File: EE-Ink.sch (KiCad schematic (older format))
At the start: 26 parts, among them U1 ED060SC4

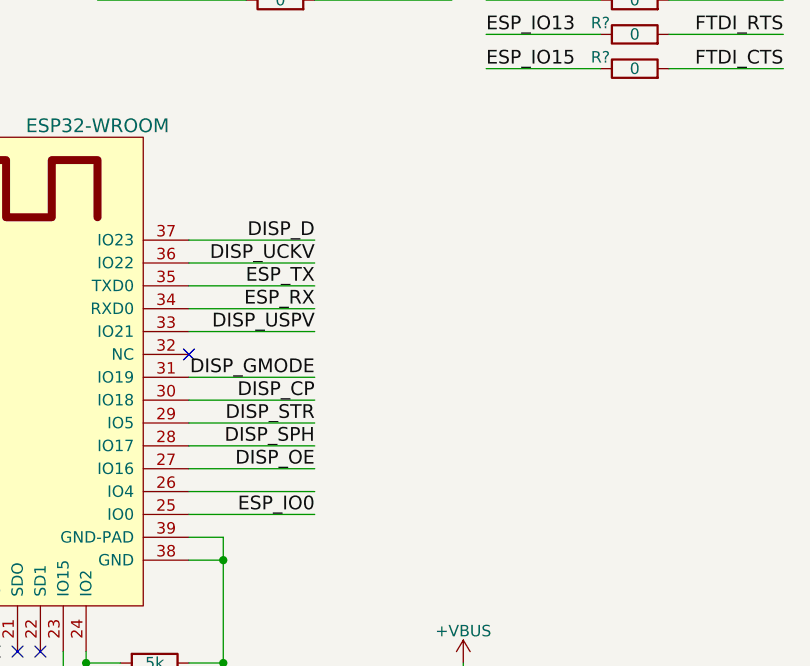
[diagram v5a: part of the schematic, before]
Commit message: Added status LED.
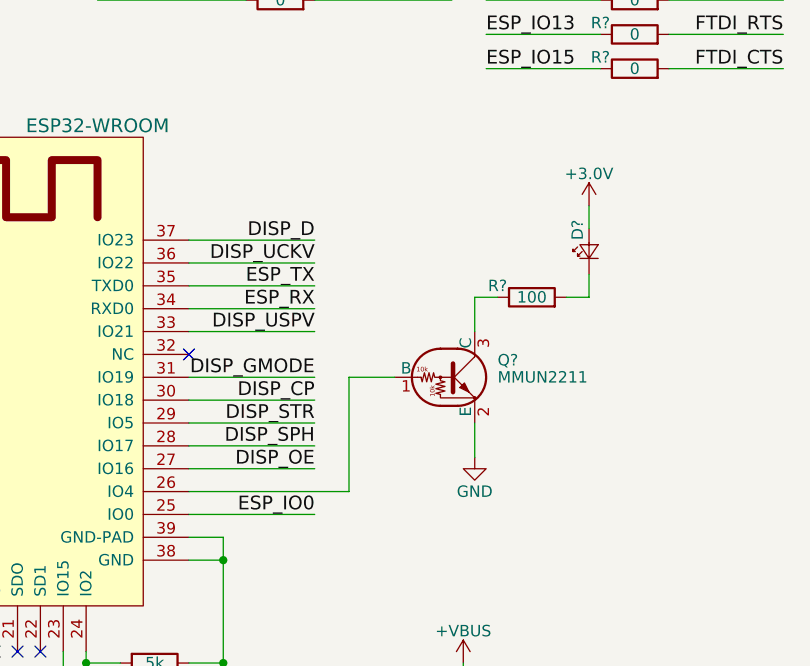
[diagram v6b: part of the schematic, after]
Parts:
- added D?: LED_Small, symbol LED_Small
- added Q?: MMUN2211, symbol DTC114E
- added R?: 100, symbol R
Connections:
- net +3.0V: now also D?.2 (A)
- net GND: now also Q?.2 (E)
- net at U?.26 (IO4): now also Q?.1 (B)
- new net: Q?.3 (C), R?.1
- new net: D?.1 (K), R?.2
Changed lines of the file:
@@
 	8300 3250 8850 3250
 Wire Wire Line
-	8300 3350 8850 3350
+	8300 3350 9000 3350
 $Comp
 L C_Small C?
@@
 	5350 4150 5350 4050
 Connection ~ 5350 4050
+$Comp
+L DTC114E Q?
+U 1 1 58E4DFD0
+P 9450 2850
+F 0 "Q?" H 9650 2925 50  0000 L CNN
+F 1 "MMUN2211" H 9650 2850 50  0000 L CNN
+F 2 "" H 9450 2850 50  0001 L CNN
+F 3 "" H 9450 2850 50  0001 L CNN
+	1    9450 2850
+	1    0    0    -1
+$EndComp
+$Comp
+L GND #PWR?
+U 1 1 58E4F157
+P 9550 3200
+F 0 "#PWR?" H 9550 2950 50  0001 C CNN
+F 1 "GND" H 9550 3050 50  0000 C CNN
+F 2 "" H 9550 3200 50  0001 C CNN
+F 3 "" H 9550 3200 50  0001 C CNN
+	1    9550 3200
+	1    0    0    -1
+$EndComp
+Wire Wire Line
+	9550 3050 9550 3200
+Wire Wire Line
+	9200 2850 9000 2850
+Wire Wire Line
+	9000 2850 9000 3350
+$Comp
+L R R?
+U 1 1 58E50804
+P 9800 2500
+F 0 "R?" V 9850 2650 50  0000 C CNN
+F 1 "100" V 9800 2500 50  0000 C CNN
+F 2 "" V 9730 2500 50  0001 C CNN
+F 3 "" H 9800 2500 50  0001 C CNN
+	1    9800 2500
+	0    -1   -1   0
+$EndComp
+Wire Wire Line
+	9550 2650 9550 2500
+Wire Wire Line
+	9550 2500 9650 2500
+$Comp
+L LED_Small D?
+U 1 1 58E50A54
+P 10050 2300
+F 0 "D?" H 10100 2350 50  0000 L CNN
+F 1 "LED_Small" H 9875 2200 50  0001 L CNN
+F 2 "" V 10050 2300 50  0001 C CNN
+F 3 "" V 10050 2300 50  0001 C CNN
+	1    10050 2300
+	0    -1   -1   0
+$EndComp
+Wire Wire Line
+	10050 2400 10050 2500
+Wire Wire Line
+	10050 2500 9950 2500
+$Comp
+L +3.0V #PWR?
+U 1 1 58E512ED
+P 10050 2100
+F 0 "#PWR?" H 10050 1950 50  0001 C CNN
+F 1 "+3.0V" H 10050 2240 50  0000 C CNN
+F 2 "" H 10050 2100 50  0001 C CNN
+F 3 "" H 10050 2100 50  0001 C CNN
+	1    10050 2100
+	1    0    0    -1
+$EndComp
+Wire Wire Line
+	10050 2100 10050 2200
 $EndSCHEMATC

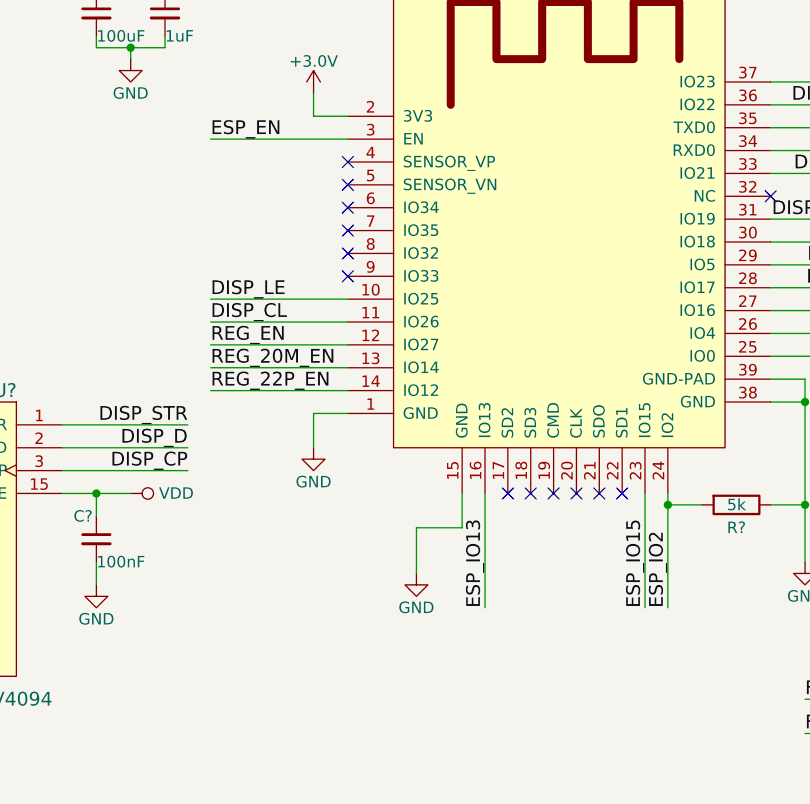
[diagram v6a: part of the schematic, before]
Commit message: Added some labels for the unused pins.
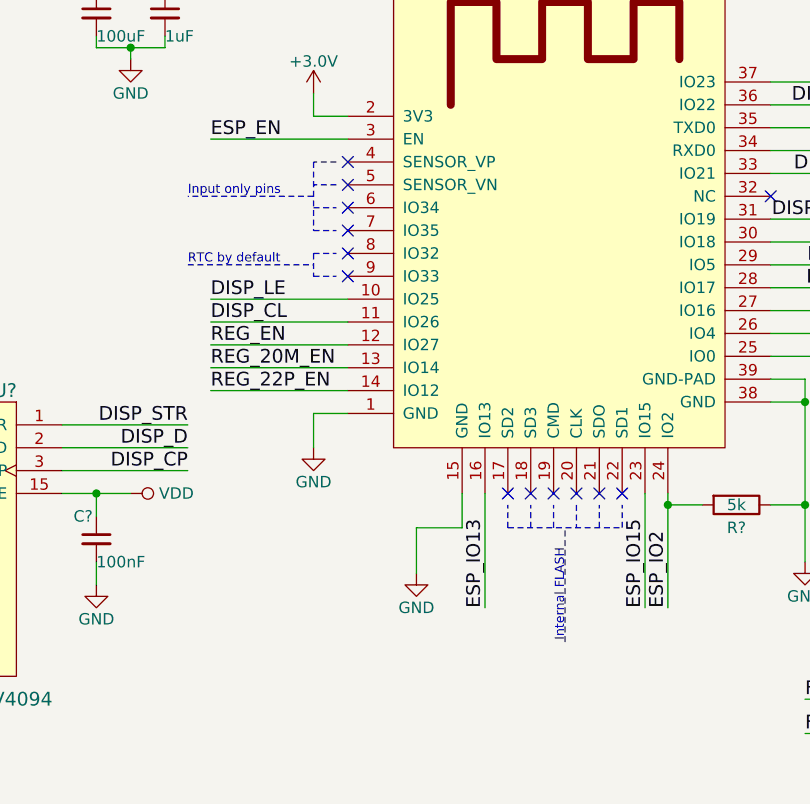
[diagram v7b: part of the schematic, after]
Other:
- note added: "Input only pins"
- note added: "Internal FLASH"
- note added: "RTC by default"
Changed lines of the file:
@@
 Wire Wire Line
 	10050 2100 10050 2200
+Text Notes 5750 2750 0    40   ~ 0
+Input only pins
+Wire Notes Line
+	6400 2600 6300 2600
+Wire Notes Line
+	6300 2600 6300 2900
+Wire Notes Line
+	6300 2750 5750 2750
+Wire Notes Line
+	6400 2700 6300 2700
+Wire Notes Line
+	6300 2800 6400 2800
+Wire Notes Line
+	6300 2900 6400 2900
+Text Notes 5750 3050 0    40   ~ 0
+RTC by default
+Wire Notes Line
+	5750 3050 6300 3050
+Wire Notes Line
+	6300 3000 6300 3100
+Wire Notes Line
+	6300 3000 6400 3000
+Wire Notes Line
+	6300 3100 6400 3100
+Text Notes 7400 4700 1    40   ~ 0
+Internal FLASH
+Wire Notes Line
+	7150 4200 7650 4200
+Wire Notes Line
+	7150 4200 7150 4100
+Wire Notes Line
+	7250 4200 7250 4100
+Wire Notes Line
+	7350 4200 7350 4100
+Wire Notes Line
+	7550 4200 7550 4100
+Wire Notes Line
+	7650 4200 7650 4100
+Wire Notes Line
+	7400 4700 7400 4200
+Wire Notes Line
+	7450 4100 7450 4200
 $EndSCHEMATC

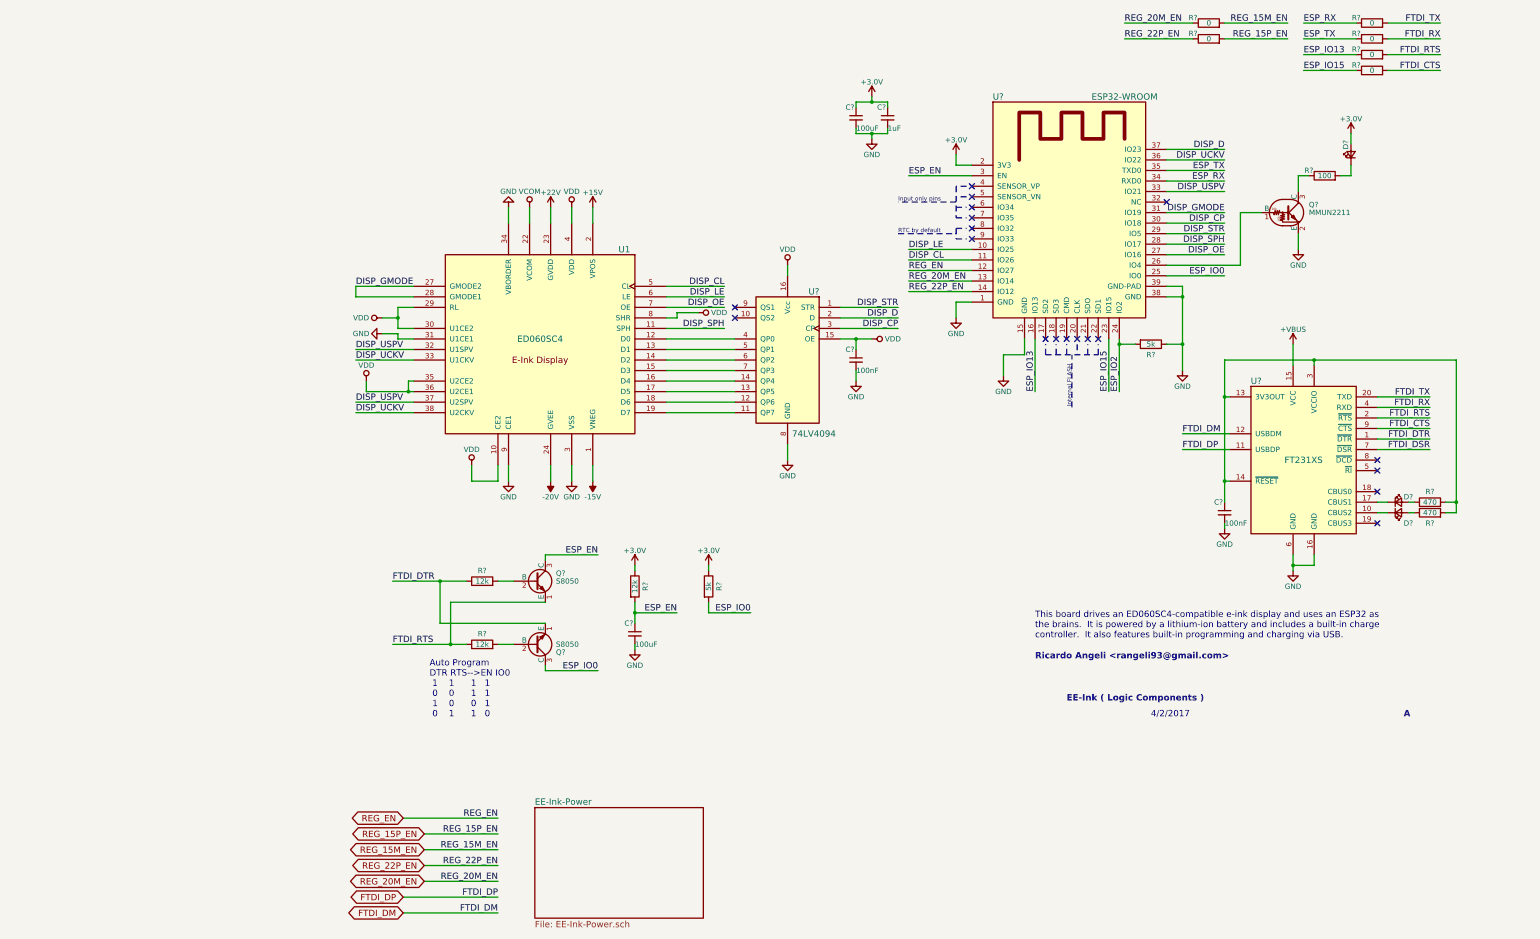
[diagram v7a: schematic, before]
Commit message: Finished reviewing schematic.  Re-annotated all components.
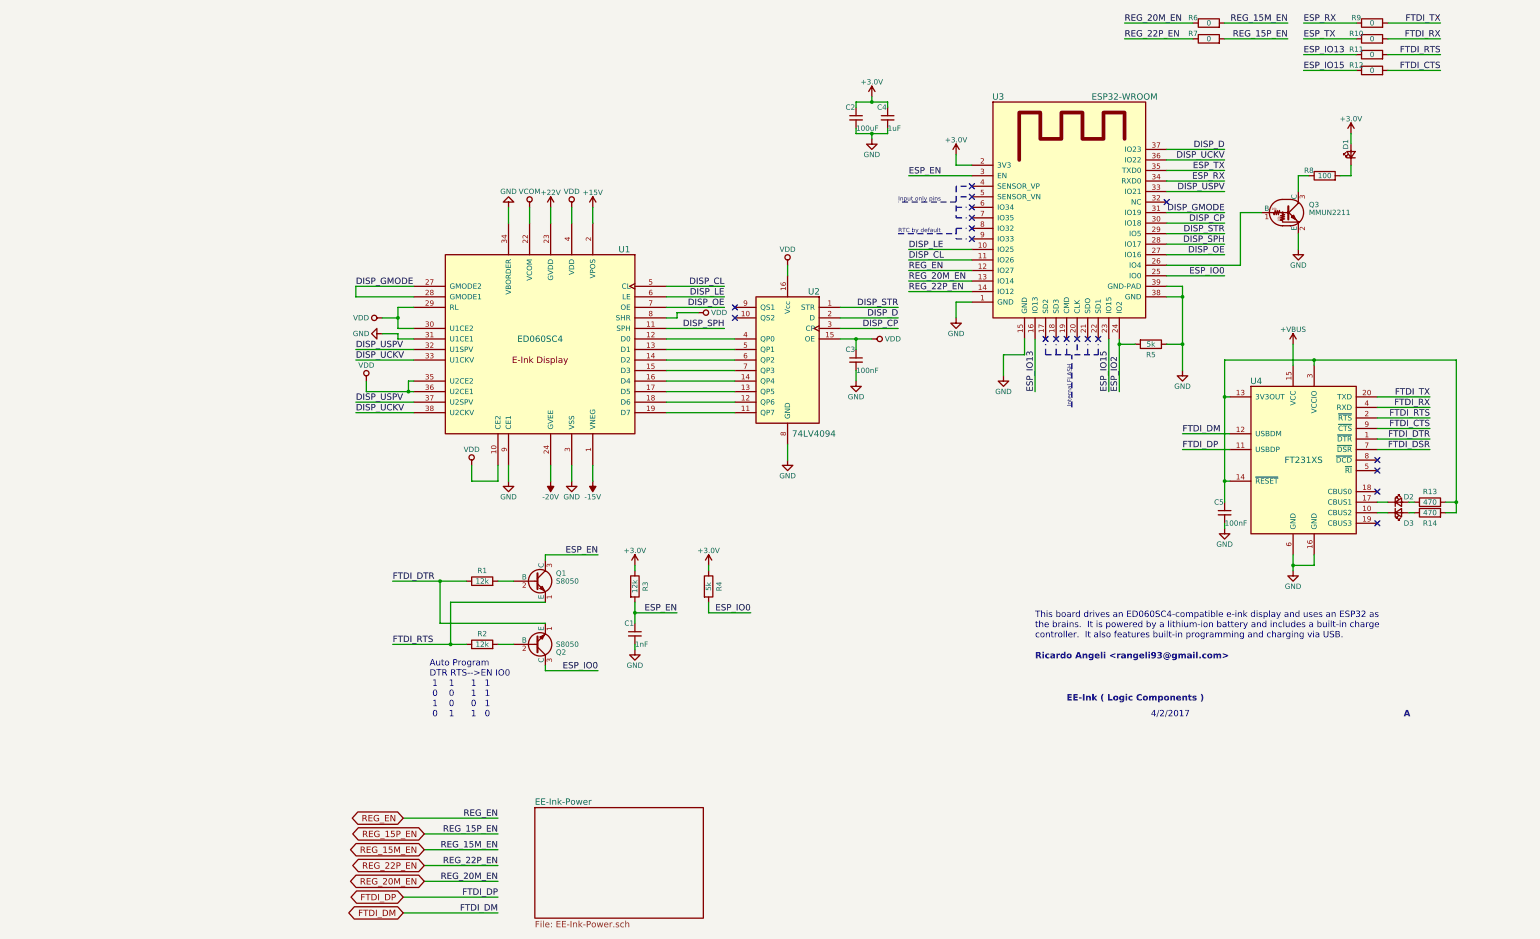
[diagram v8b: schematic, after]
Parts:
- C1: renamed from C?; value 100uF -> 1nF
- gave numbers to parts that had none: 27
